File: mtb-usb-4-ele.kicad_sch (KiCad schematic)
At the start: 77 parts, among them J1 USB_C_Receptacle_USB2.0, J2 PROG/DEBUG, J3 Conn_01x06, J4 RJ12, J5 RJ12, J6 MV133-3,5-V-L, J7 MV133-3,5-V-L, J8 Conn_01x02, U1 STM32F103C8Tx, U2 AMS1117-3.3, U3 ADM2483xRW, U4 ADUM1250, U6 LM78M05_TO252, U7 INA219AxDCN, Y1 8 MHz

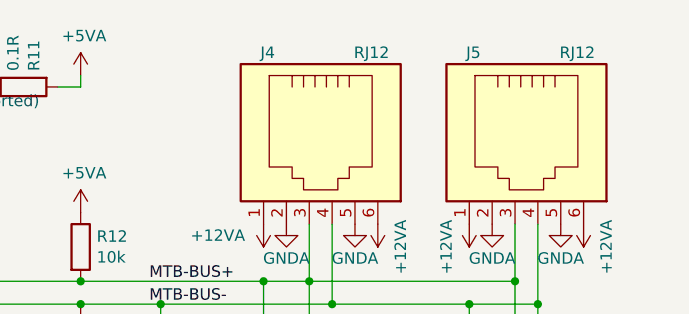
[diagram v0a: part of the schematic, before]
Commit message: Note RJ12 GME & TME part names.
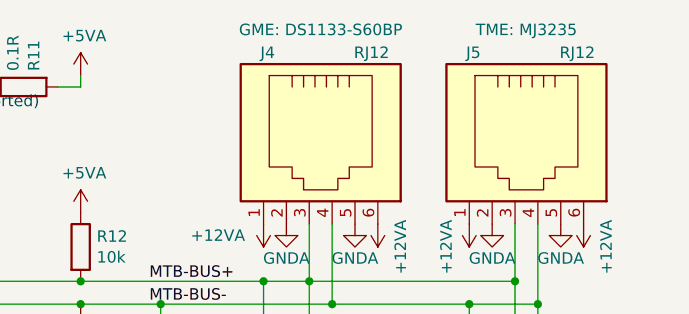
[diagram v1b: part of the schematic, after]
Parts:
- J4, J5: GME (none) -> DS1133-S60BP; TME (none) -> MJ3235
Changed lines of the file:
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@@
+			)
+		)
+		(property "TME" "MJ3235"
+			(at 271.78 13.97 90)
+			(show_name yes)
+			(effects
+				(font
+					(size 1.27 1.27)
+				)
+			)
+		)
+		(property "GME" "DS1133-S60BP"
+			(at 248.92 13.97 90)
+			(show_name yes)
+			(effects
+				(font
+					(size 1.27 1.27)
+				)
 			)
 		)
@@
 			(at 247.65 25.4 90)
 			(effects
+				(font
+					(size 1.27 1.27)
+				)
+				(hide yes)
+			)
+		)
+		(property "TME" "MJ3235"
+			(at 247.65 25.4 90)
+			(effects
+				(font
+					(size 1.27 1.27)
+				)
+				(hide yes)
+			)
+		)
+		(property "GME" "DS1133-S60BP"
+			(at 247.65 25.4 90)
+			(effects
